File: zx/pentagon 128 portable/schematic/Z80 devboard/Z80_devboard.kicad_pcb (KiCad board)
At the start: 2 copper layers, 58.7 x 60.7 mm, 38 parts, among them IC1 Z84C0020AEG, IC2 TXB0108PWR, IC3 TXB0108PWR, IC4 TXB0108PWR, IC5 TXB0108PWR, IC6 TXB0108PWR, J1 Conn_01x08, J2 Conn_01x16, J3 Conn_01x11, U1 LD1117S50TR_SOT223, U2 LD1117S33TR_SOT223

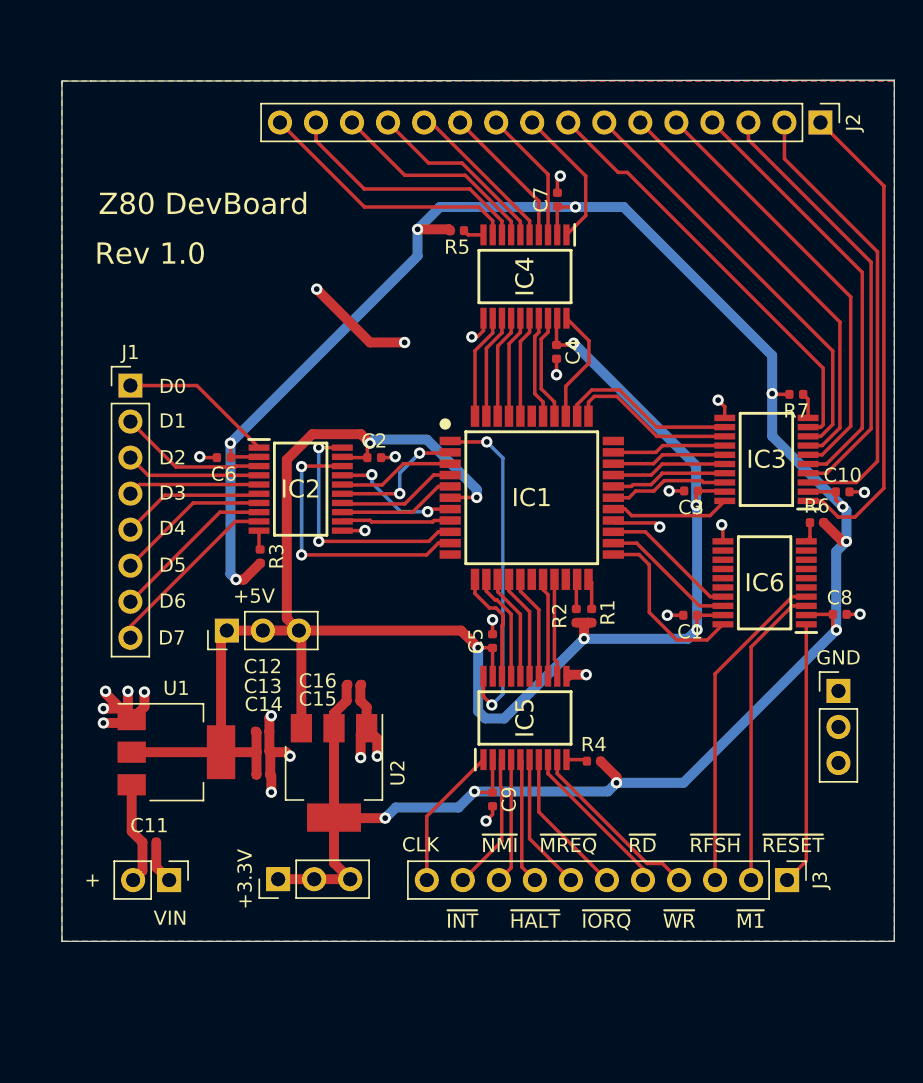
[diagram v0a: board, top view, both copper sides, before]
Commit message: reorganizing. finished ram and keyboard, updated z80
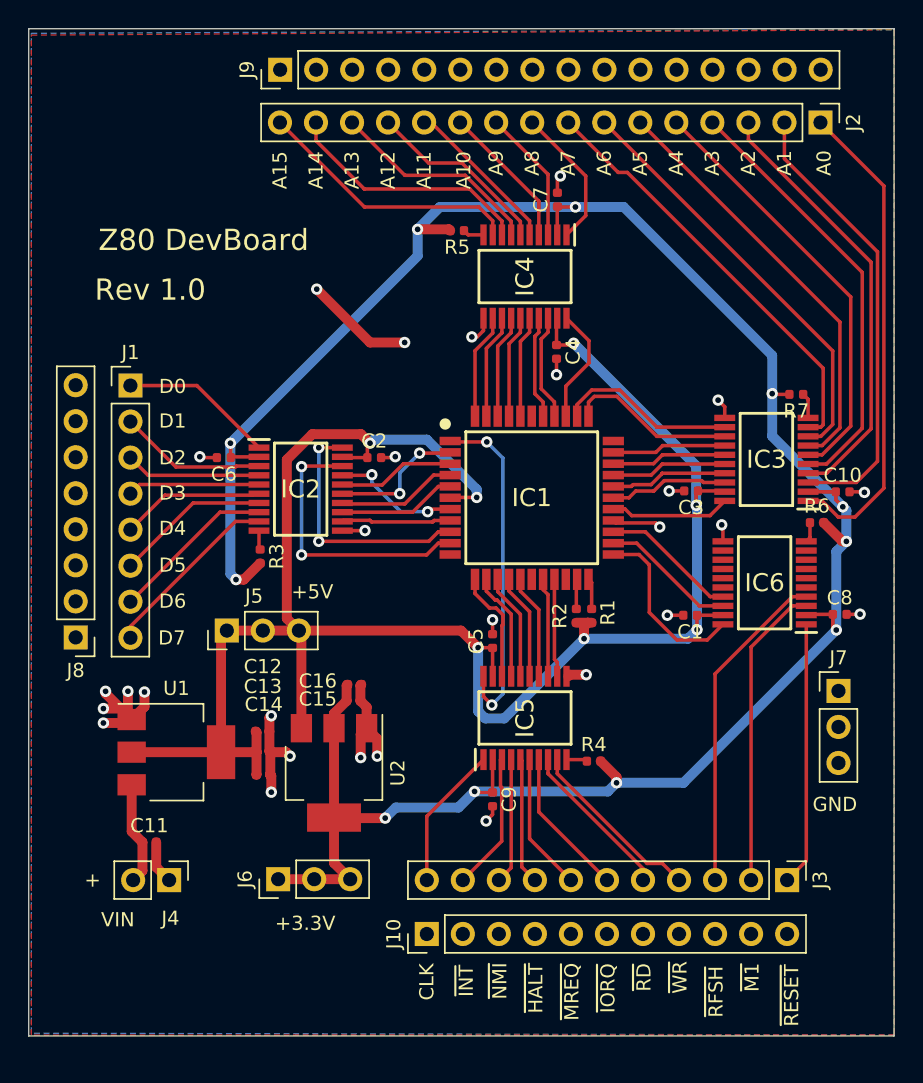
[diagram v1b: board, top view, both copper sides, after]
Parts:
- added J10: Conn_01x11, Connector_PinHeader_2.54mm:PinHeader_1x11_P2.54mm_Vertical, F.Cu at (103.1, 115.8)
- added J8: Conn_01x08, Connector_PinHeader_2.54mm:PinHeader_1x08_P2.54mm_Vertical, F.Cu at (78.3, 94.9)
- added J9: Conn_01x16, Connector_PinHeader_2.54mm:PinHeader_1x16_P2.54mm_Vertical, F.Cu at (92.7, 54.9)
- renumbered VIN to J4, +5V to J5, +3.3V to J6, GND to J7
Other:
- board size 58.7 x 60.7 mm -> 61 x 71 mm
- board text added: "+3.3V"
- board text added: "+5V"
- board text added: "A0"
- board text added: "A1"
- board text added: "A10"
- board text added: "A11"
- board text added: "A12"
- board text added: "A13"
- board text added: "A14"
- board text added: "A15"
- board text added: "A2"
- board text added: "A3"
- board text added: "A4"
- board text added: "A5"
- board text added: "A6"
- board text added: "A7"
- board text added: "A8"
- board text added: "A9"
- board text added: "GND"
- board text added: "VIN"

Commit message: added z80 pdip. updated all boards
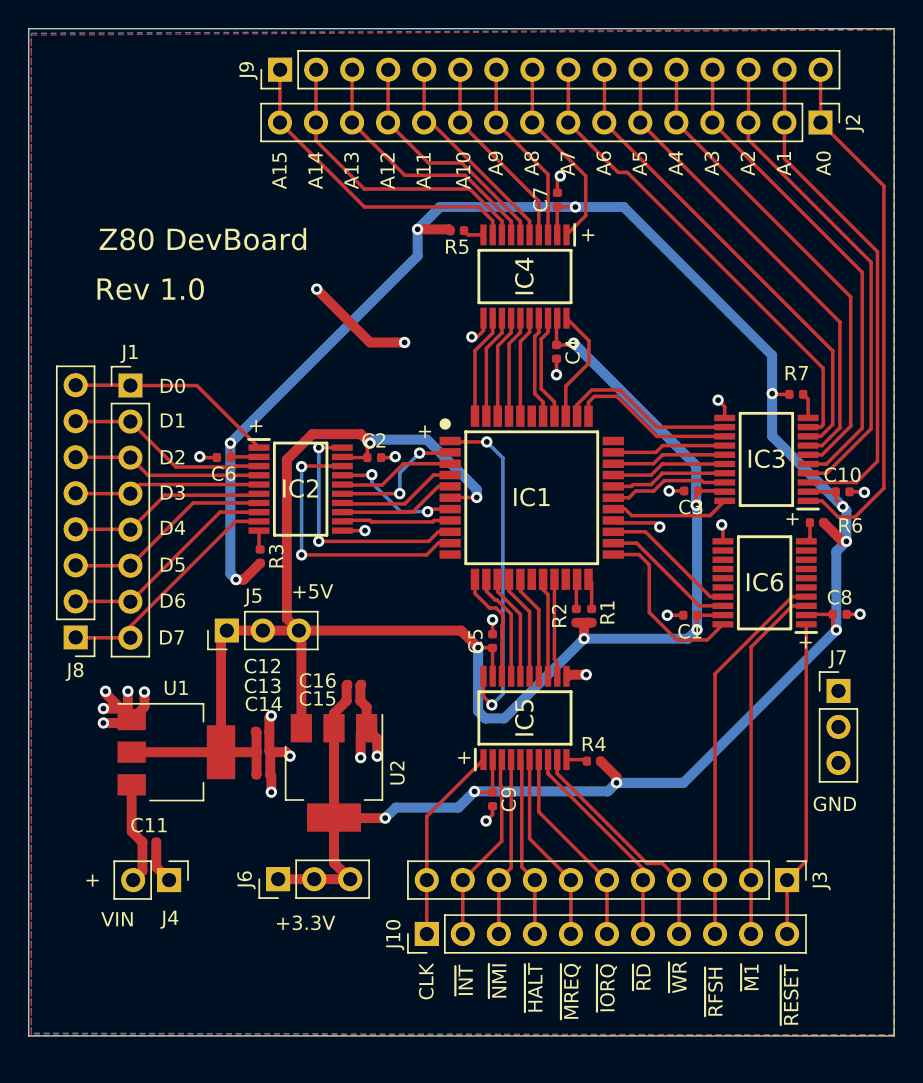
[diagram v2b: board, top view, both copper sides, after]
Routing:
- net /D6: track 11.7 -> 15.5 mm
- net /D4: track 10.1 -> 14.0 mm
- net /D2: track 9.58 -> 13.5 mm
- net /D0: track 10.9 -> 14.7 mm
- net /D7: track 12.9 -> 16.8 mm
- net /D5: track 10.9 -> 14.8 mm
- net /D3: track 9.33 -> 13.2 mm
- net /D1: track 10.4 -> 14.3 mm
- net /~WR: track 12.7 -> 16.5 mm
- net /~RFSH: track 23.2 -> 27.0 mm
- net /~RESET: track 18.6 -> 22.4 mm
- net /~RD: track 11.3 -> 15.1 mm
- net /~NMI: track 8.85 -> 12.6 mm
- net /~MREQ: track 9.70 -> 13.5 mm
- net /~M1: track 21.5 -> 25.3 mm
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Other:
- board text added: "JLCJLCJLCJLC"
